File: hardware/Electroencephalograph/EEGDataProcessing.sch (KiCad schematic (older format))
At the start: 1 part, among them U3 TMS320LF2406PZ

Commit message: placing components groups
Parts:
- removed U3: TMS320LF2406PZ, Package_QFP:LQFP-144_20x20mm_P0.5mm, symbol DSP_Texas:TMS320LF2406PZ
- added U3: DSPIC33FJ128MC710A, Package_QFP:TQFP-100-1EP_14x14mm_P0.5mm_EP5x5mm, symbol DSP_Microchip_DSPIC33:DSPIC33FJ128MC710A
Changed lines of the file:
@@
 $EndDescr
 $Comp
-L DSP_Texas:TMS320LF2406PZ U?
-U 1 1 5E1478E4
-P 4500 3800
-AR Path="/5DF61103/5E1478E4" Ref="U?"  Part="1"
-AR Path="/5E142744/5E1478E4" Ref="U3"  Part="1"
-F 0 "U3" H 4500 6681 50  0000 C CNN
-F 1 "TMS320LF2406PZ" H 4500 6590 50  0000 C CNN
-F 2 "Package_QFP:LQFP-144_20x20mm_P0.5mm" H 4500 3800 50  0001 C CNN
-F 3 "http://www.ti.com/lit/ds/symlink/tms320lf2406.pdf" H 4500 3800 50  0001 C CNN
-	1    4500 3800
+L DSP_Microchip_DSPIC33:DSPIC33FJ128MC710A U3
+U 1 1 5E1164DA
+P 3800 3650
+F 0 "U3" H 3800 861 50  0000 C CNN
+F 1 "DSPIC33FJ128MC710A" H 3800 770 50  0000 C CNN
+F 2 "Package_QFP:TQFP-100-1EP_14x14mm_P0.5mm_EP5x5mm" H 3800 3950 50  0001 C CNN
+F 3 "http://ww1.microchip.com/downloads/en/DeviceDoc/70594C.pdf" H 3800 3950 50  0001 C CNN
+	1    3800 3650
 	1    0    0    -1
 $EndComp

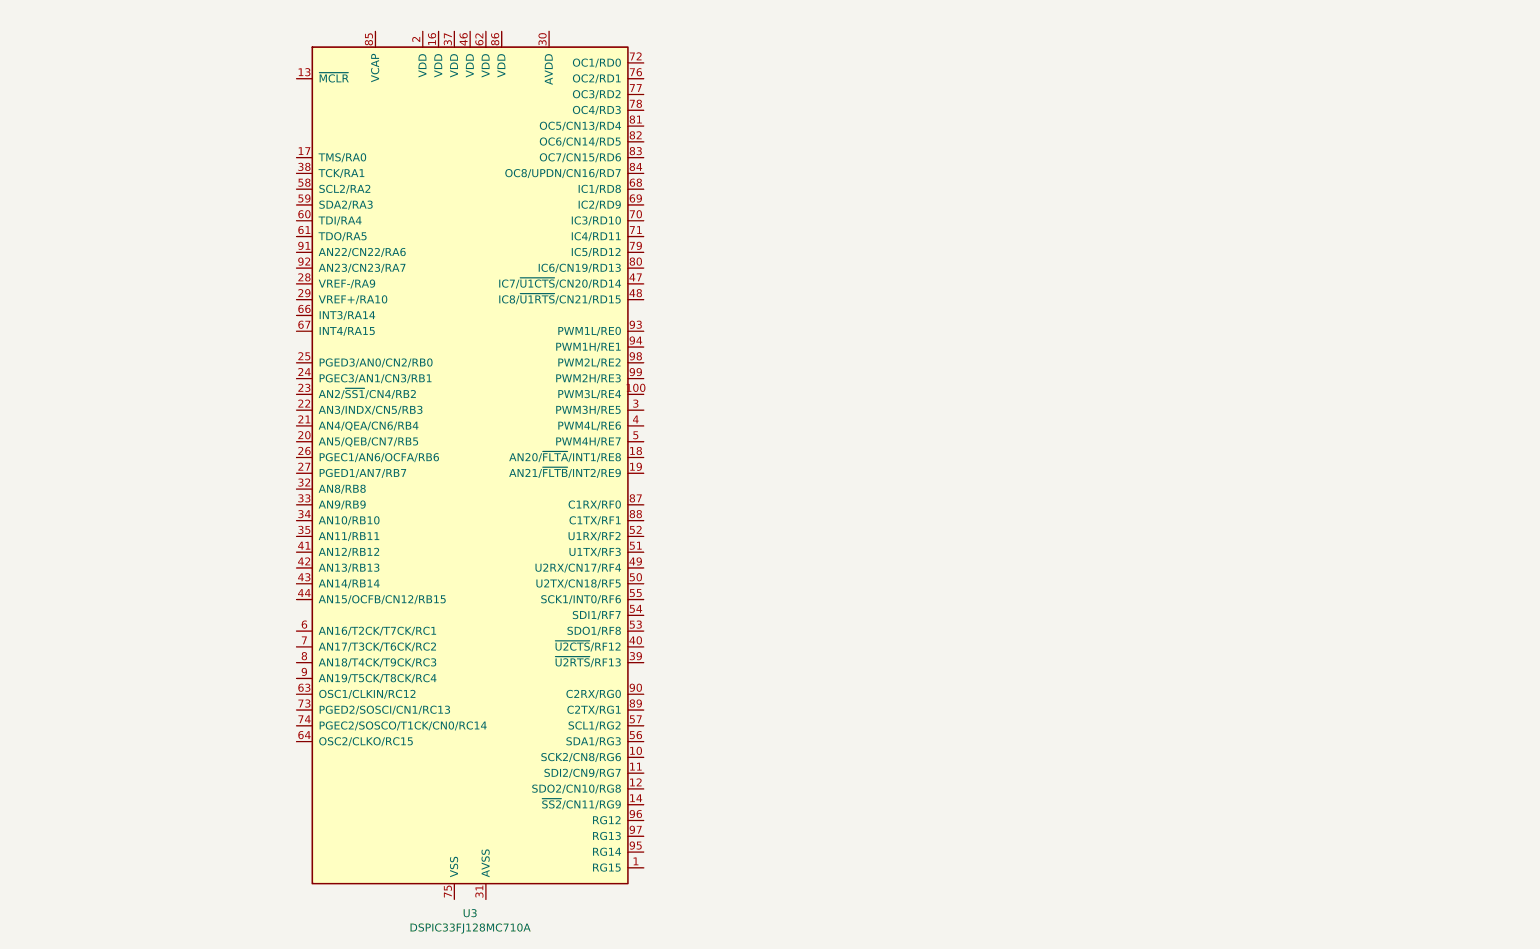
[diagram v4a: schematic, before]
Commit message: added procesing unit
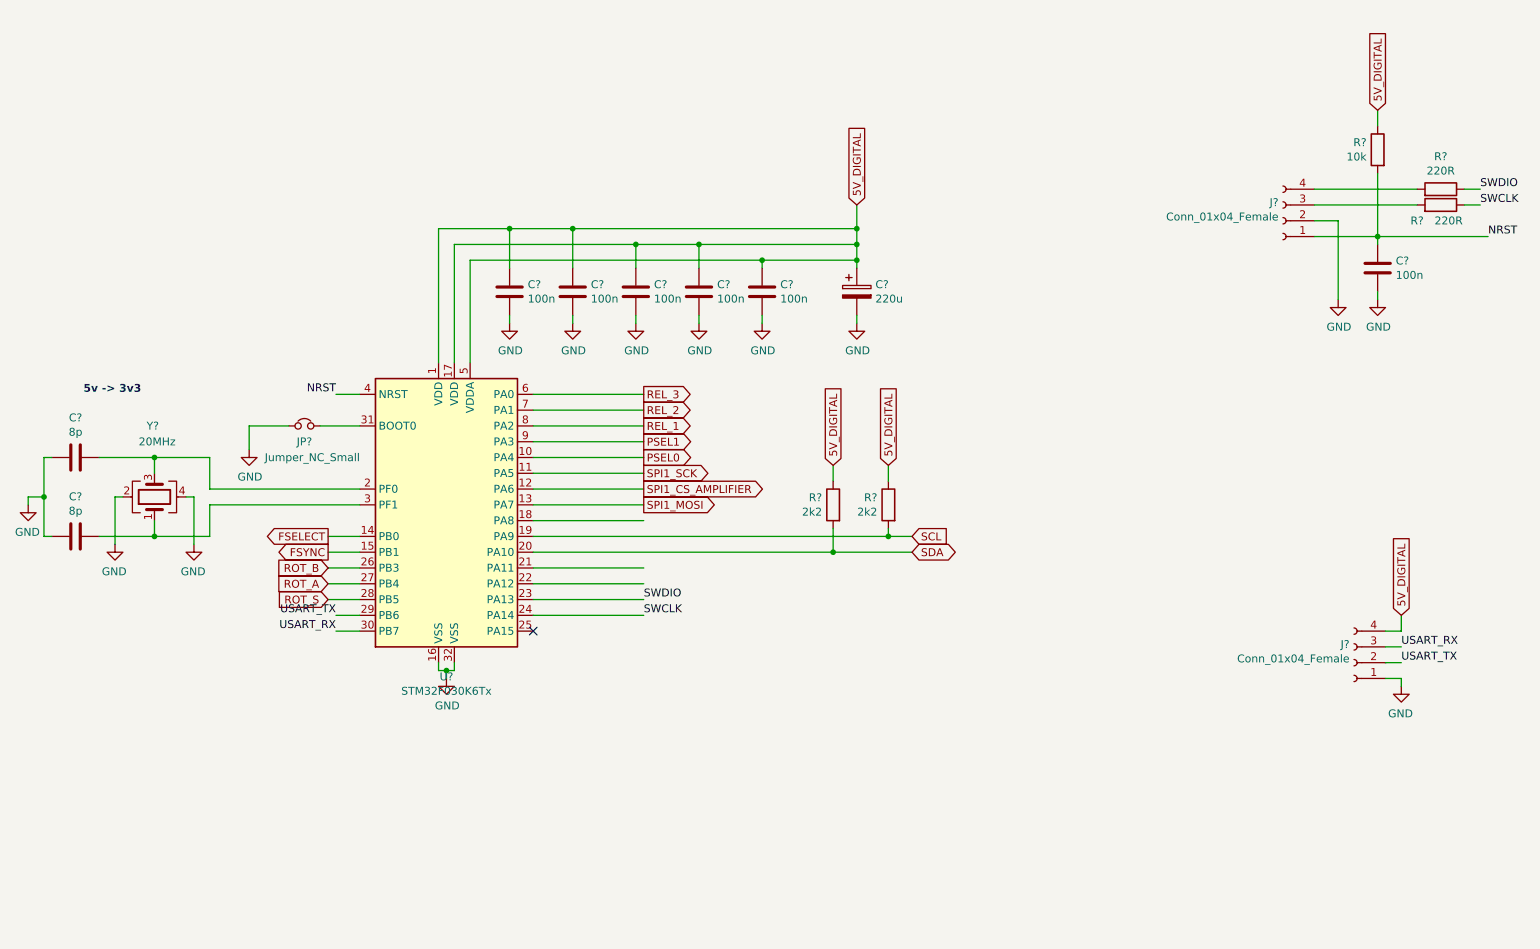
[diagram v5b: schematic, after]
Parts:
- removed U3: DSPIC33FJ128MC710A, Package_QFP:TQFP-100-1EP_14x14mm_P0.5mm_EP5x5mm, symbol DSP_Microchip_DSPIC33:DSPIC33FJ128MC710A
- added C? (x6): 100n, Capacitor_SMD:C_0402_1005Metric, symbol Device:C
- added C? (x2): 8p, Capacitor_SMD:C_0402_1005Metric, symbol Device:C
- added C?: 220u, Capacitor_SMD:CP_Elec_6.3x5.8, symbol Device:CP
- added J? (x2): Conn_01x04_Female, Connector_PinHeader_2.54mm:PinHeader_1x04_P2.54mm_Vertical, symbol Connector:Conn_01x04_Female
- added JP?: Jumper_NC_Small, Jumper:SolderJumper-2_P1.3mm_Bridged2Bar_RoundedPad1.0x1.5mm, symbol Device:Jumper_NC_Small
- added R?: 2k2, Resistor_SMD:R_0402_1005Metric, symbol Device:R
- added R?: 2k2, Resistor_SMD:R_0805_2012Metric_Pad1.15x1.40mm_HandSolder, symbol Device:R
- added R?: 10k, Resistor_SMD:R_0402_1005Metric, symbol Device:R
- added R? (x2): 220R, Resistor_SMD:R_0402_1005Metric, symbol Device:R
- added U?: STM32F030K6Tx, Package_QFP:LQFP-32_7x7mm_P0.8mm, symbol MCU_ST_STM32F0:STM32F030K6Tx
- added Y?: 20MHz, Oscillator:Oscillator_SMD_EuroQuartz_XO53-4Pin_5.0x3.2mm, symbol Device:Crystal_GND24
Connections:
- new net: C?.2, U?.2 (PF0), Y?.3
- new net: C?.2, U?.3 (PF1), Y?.1
- new net: JP?.2, U?.31 (BOOT0)
- new net: J?.4 (Pin_4), R?.2
- new net: J?.3 (Pin_3), R?.2
- new net 5V_DIGITAL: C?.1, C?.1, C?.1, C?.1, C?.1, C?.1, J?.4 (Pin_4), R?.1, R?.1, R?.1, U?.1 (VDD), U?.17 (VDD), U?.5 (VDDA)
- new net FSELECT: U?.14 (PB0)
- new net FSYNC: U?.15 (PB1)
- new net GND: C?.1, C?.1, C?.2, C?.2, C?.2, C?.2, C?.2, C?.2, C?.2, J?.1 (Pin_1), J?.2 (Pin_2), JP?.1, U?.16 (VSS), U?.32 (VSS), Y?.2, Y?.4
- new net NRST: C?.1, J?.1 (Pin_1), R?.2, U?.4 (NRST)
- new net PSEL0: U?.10 (PA4)
- new net PSEL1: U?.9 (PA3)
- new net REL_1: U?.8 (PA2)
- new net REL_2: U?.7 (PA1)
- new net REL_3: U?.6 (PA0)
- new net ROT_A: U?.27 (PB4)
- new net ROT_B: U?.26 (PB3)
- new net ROT_S: U?.28 (PB5)
- new net SCL: R?.2, U?.19 (PA9)
- new net SDA: R?.2, U?.20 (PA10)
- new net SPI1_CS_AMPLIFIER: U?.12 (PA6)
- new net SPI1_MOSI: U?.13 (PA7)
- new net SPI1_SCK: U?.11 (PA5)
- new net SWCLK: R?.1, U?.24 (PA14)
- new net SWDIO: R?.1, U?.23 (PA13)
- new net USART_RX: J?.3 (Pin_3), U?.30 (PB7)
- new net USART_TX: J?.2 (Pin_2), U?.29 (PB6)
- no-connect marks 0 -> 1
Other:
- note added: "5v -> 3v3"

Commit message: eeg digital part routing
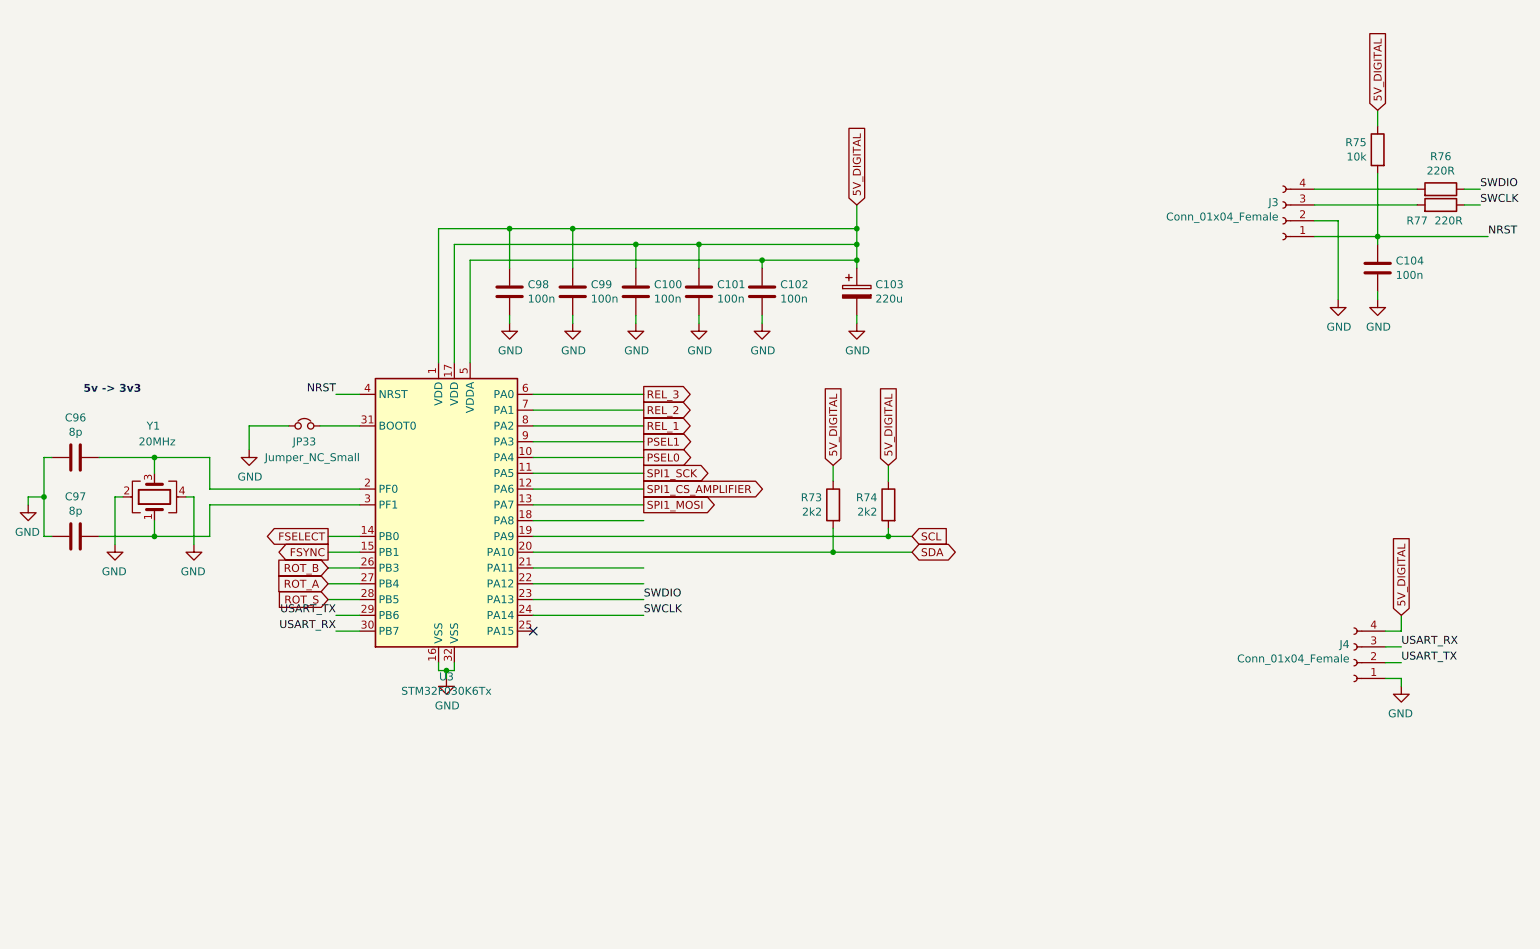
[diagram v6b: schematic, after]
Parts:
- gave numbers to parts that had none: 19

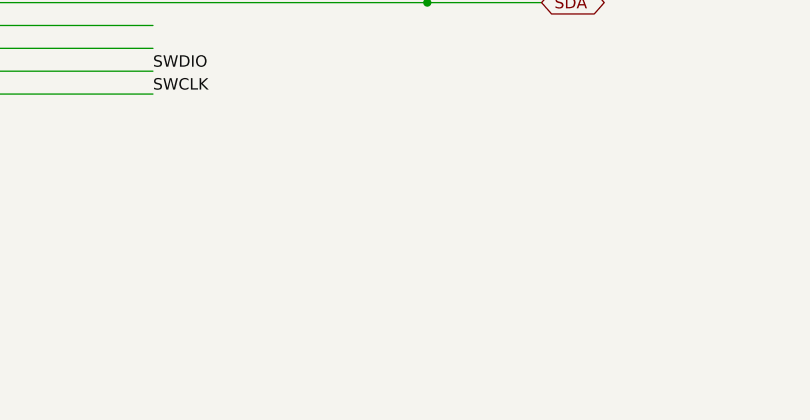
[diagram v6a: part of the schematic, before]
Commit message: routing of analog power supply
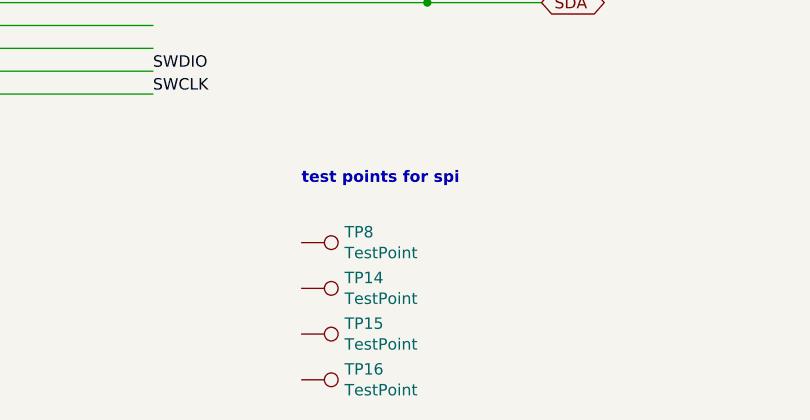
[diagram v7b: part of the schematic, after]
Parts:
- added TP14, TP15, TP16, TP8: TestPoint, TestPoint:TestPoint_Pad_D1.0mm, symbol Connector:TestPoint
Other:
- note added: "test points for spi"
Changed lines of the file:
@@
 Wire Wire Line
 	3100 4250 2900 4250
-Text GLabel 2900 4150 0    50   Output ~ 0
-FSYNC
 Wire Wire Line
 	3100 4150 2900 4150
@@
 Text GLabel 4900 3850 2    50   Output ~ 0
 SPI1_MOSI
-Text GLabel 4900 3150 2    50   Output ~ 0
-REL_3
 Text GLabel 6450 3600 1    50   Input ~ 0
 5V_DIGITAL
@@
 Text GLabel 6600 4050 2    50   Input ~ 0
 SCL
-Text GLabel 2900 4350 0    50   Input ~ 0
-ROT_A
-Text GLabel 2900 4250 0    50   Input ~ 0
-ROT_B
 Text GLabel 2900 4450 0    50   Input ~ 0
 ROT_S
@@
 Text GLabel 6600 4150 2    50   BiDi ~ 0
 SDA
-Text GLabel 4900 3250 2    50   Output ~ 0
-REL_2
-Text GLabel 4900 3350 2    50   Output ~ 0
-REL_1
-Text GLabel 2900 4050 0    50   Output ~ 0
-FSELECT
-Text GLabel 4900 3450 2    50   Output ~ 0
-PSEL1
-Text GLabel 4900 3550 2    50   Output ~ 0
-PSEL0
 $Comp
 L Device:R R?
@@
 Wire Wire Line
 	9150 2150 9550 2150
+$Comp
+L Connector:TestPoint TP?
+U 1 1 5E21FE22
+P 5550 5800
+AR Path="/5DF61103/5E21FE22" Ref="TP?"  Part="1"
+AR Path="/5E142744/5E21FE22" Ref="TP16"  Part="1"
+F 0 "TP16" V 5504 5988 50  0000 L CNN
+F 1 "TestPoint" V 5595 5988 50  0000 L CNN
+F 2 "TestPoint:TestPoint_Pad_D1.0mm" H 5750 5800 50  0001 C CNN
+F 3 "~" H 5750 5800 50  0001 C CNN
+	1    5550 5800
+	0    1    1    0
+$EndComp
+$Comp
+L Connector:TestPoint TP?
+U 1 1 5E21FE28
+P 5550 5600
+AR Path="/5DF61103/5E21FE28" Ref="TP?"  Part="1"
+AR Path="/5E142744/5E21FE28" Ref="TP15"  Part="1"
+F 0 "TP15" V 5504 5788 50  0000 L CNN
+F 1 "TestPoint" V 5595 5788 50  0000 L CNN
+F 2 "TestPoint:TestPoint_Pad_D1.0mm" H 5750 5600 50  0001 C CNN
+F 3 "~" H 5750 5600 50  0001 C CNN
+	1    5550 5600
+	0    1    1    0
+$EndComp
+$Comp
+L Connector:TestPoint TP?
+U 1 1 5E21FE2E
+P 5550 5400
+AR Path="/5DF61103/5E21FE2E" Ref="TP?"  Part="1"
+AR Path="/5E142744/5E21FE2E" Ref="TP14"  Part="1"
+F 0 "TP14" V 5504 5588 50  0000 L CNN
+F 1 "TestPoint" V 5595 5588 50  0000 L CNN
+F 2 "TestPoint:TestPoint_Pad_D1.0mm" H 5750 5400 50  0001 C CNN
+F 3 "~" H 5750 5400 50  0001 C CNN
+	1    5550 5400
+	0    1    1    0
+$EndComp
+$Comp
+L Connector:TestPoint TP?
+U 1 1 5E21FE34
+P 5550 5200
+AR Path="/5DF61103/5E21FE34" Ref="TP?"  Part="1"
+AR Path="/5E142744/5E21FE34" Ref="TP8"  Part="1"
+F 0 "TP8" V 5504 5388 50  0000 L CNN
+F 1 "TestPoint" V 5595 5388 50  0000 L CNN
+F 2 "TestPoint:TestPoint_Pad_D1.0mm" H 5750 5200 50  0001 C CNN
+F 3 "~" H 5750 5200 50  0001 C CNN
+	1    5550 5200
+	0    1    1    0
+$EndComp
+Text GLabel 2900 4350 0    50   Input ~ 0
+ROT_A
+Text GLabel 2900 4250 0    50   Input ~ 0
+ROT_B
+Text GLabel 2900 4150 0    50   Output ~ 0
+FSYNC
+Text GLabel 2900 4050 0    50   Output ~ 0
+FSELECT
+Text GLabel 4900 3550 2    50   Output ~ 0
+PSEL0
+Text GLabel 4900 3450 2    50   Output ~ 0
+PSEL1
+Text GLabel 4900 3350 2    50   Output ~ 0
+REL_1
+Text GLabel 4900 3250 2    50   Output ~ 0
+REL_2
+Text GLabel 4900 3150 2    50   Output ~ 0
+REL_3
+Text Notes 5550 4950 0    50   ~ 10
+test points for spi
 $EndSCHEMATC
